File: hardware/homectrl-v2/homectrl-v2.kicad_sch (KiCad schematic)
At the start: 127 parts, among them J1 Barrel_Jack, J2 PUMP1_CONN, J3 PUMP2_CONN, J4 STEP_CONN, J5 USB_C_CONN, J6 SMS1_CONN, J7 ALS_CONN, J8 FSW1_CONN, Q1 AO3407A, Q2 2N7002, Q3 ZXMN3A01ZTA, Q4 ZXMN3A01ZTA, Q5 AO3400A, SW1 S3_RESET_SW, SW2 S3_BOOT_SW, U1 TPS5405DR, U2 MCP1826S, U3 DMP4065S-7, U4 ESP32-S3-WROOM-1, U5 TMC2209, U7 TPD4E001DRLR, U8 TPD2E001DRLR, U9 SI2347DS-T1-GE3

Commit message: misc work
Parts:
- removed R37: 13k, Resistor_SMD:R_0402_1005Metric, symbol Device:R
- removed R38: 20K, Resistor_SMD:R_0402_1005Metric, symbol Device:R
- Q3, Q4: footprint ZXMN3_DIO -> Package_TO_SOT_SMD:SOT-89-3
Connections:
- net MTR_DIR: now also U4.11 (IO18)
- net MTR_STEP: now also U4.10 (IO17)
- net S3_RXD: now also U4.12 (IO8)
- net S3_TXD: now also U4.15 (IO3)
- net SMS1_DATA: now also U4.6 (IO6), U4.7 (IO7); no longer U4.12 (IO8)
- net SMS2_DATA: no longer U4.17 (IO9)
- net STEP_DIAG: now also U4.17 (IO9)
- net STEP_ENN: now also U4.18 (IO10)
- net VCC_SENSE: no longer names the net of U4.4 (IO4)
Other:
- note added: "V = 12 ( 20 / 120 ) = 2 v V < 3V3"
- note removed: "V = 12 ( 20 / 120 ) = 2 v V = 3.3 ( 20 / 33 ) = 2 v V > 3V3"

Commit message: dasdf
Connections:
- net PUMP1_GATE is gone; now on net PUMP1_EN: R22.1
- net SMS1_DATA: now also U4.5 (IO5); no longer U4.6 (IO6), U4.7 (IO7)
- net SMS2_DATA: now also U4.6 (IO6)
- net VPLUG_SENSE: now also U4.4 (IO4); no longer U4.5 (IO5)
- net VPMP_EN: now also U4.9 (IO16)
- net PUMP1_EN: now reaches U4.8 (IO15)
- net PUMP2_GATE renamed PUMP2_EN
- net PUMP2_EN: now also U4.7 (IO7)
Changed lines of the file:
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@@
+		)
+	)
+	(global_label "VPMP_EN"
+		(shape input)
+		(at 259.08 236.22 180)
+		(fields_autoplaced yes)
+		(effects
+			(font
+				(size 1.27 1.27)
+			)
+			(justify right)
+		)
+		(property "Intersheetrefs" "${INTERSHEET_REFS}"
+			(at 247.5677 236.22 0)
+			(effects
+				(font
+					(size 1.27 1.27)
+				)
+				(justify right)
+				(hide yes)
+			)
 		)
 	)
@@
 		)
 	)
-	(global_label "VPLUG_SENSE"
-		(shape output)
-		(at 259.08 208.28 180)
-		(fields_autoplaced yes)
-		(effects
-			(font
-				(size 1.27 1.27)
-			)
-			(justify right)
-		)
-		(property "Intersheetrefs" "${INTERSHEET_REFS}"
-			(at 243.0925 208.28 0)
-			(effects
-				(font
-					(size 1.27 1.27)
-				)
-				(justify right)
-				(hide yes)
-			)
-		)
-	)
 	(global_label "MTR_STEP"
 		(shape input)
@@
 		)
 	)
+	(global_label "SMS2_DATA"
+		(shape input)
+		(at 259.08 210.82 180)
+		(fields_autoplaced yes)
+		(effects
+			(font
+				(size 1.27 1.27)
+			)
+			(justify right)
+		)
+		(property "Intersheetrefs" "${INTERSHEET_REFS}"
+			(at 245.6325 210.82 0)
+			(effects
+				(font
+					(size 1.27 1.27)
+				)
+				(justify right)
+				(hide yes)
+			)
+		)
+	)
 	(global_label "VPLUG"
 		(shape input)
@@
 				)
 				(justify left)
+				(hide yes)
+			)
+		)
+	)
+	(global_label "PUMP2_EN"
+		(shape input)
+		(at 259.08 213.36 180)
+		(fields_autoplaced yes)
+		(effects
+			(font
+				(size 1.27 1.27)
+			)
+			(justify right)
+		)
+		(property "Intersheetrefs" "${INTERSHEET_REFS}"
+			(at 246.1163 213.36 0)
+			(effects
+				(font
+					(size 1.27 1.27)
+				)
+				(justify right)
 				(hide yes)
 			)
@@
 		)
 	)
-	(global_label "PUMP2_GATE"
+	(global_label "PUMP2_EN"
 		(shape input)
 		(at 340.36 133.35 180)
@@
 		)
 		(property "Intersheetrefs" "${INTERSHEET_REFS}"
-			(at 325.4006 133.35 0)
+			(at 327.3963 133.35 0)
 			(effects
 				(font
@@
 		)
 	)
+	(global_label "SMS1_DATA"
+		(shape input)
+		(at 259.08 208.28 180)
+		(fields_autoplaced yes)
+		(effects
+			(font
+				(size 1.27 1.27)
+			)
+			(justify right)
+		)
+		(property "Intersheetrefs" "${INTERSHEET_REFS}"
+			(at 245.6325 208.28 0)
+			(effects
+				(font
+					(size 1.27 1.27)
+				)
+				(justify right)
+				(hide yes)
+			)
+		)
+	)
 	(global_label "I2C_DTA"
 		(shape input)
@@
 		)
 	)
+	(global_label "VPLUG_SENSE"
+		(shape output)
+		(at 259.08 205.74 180)
+		(fields_autoplaced yes)
+		(effects
+			(font
+				(size 1.27 1.27)
+			)
+			(justify right)
+		)
+		(property "Intersheetrefs" "${INTERSHEET_REFS}"
+			(at 243.0925 205.74 0)
+			(effects
+				(font
+					(size 1.27 1.27)
+				)
+				(justify right)
+				(hide yes)
+			)
+		)
+	)
 	(global_label "STEP_2A"
 		(shape input)
@@
 		)
 	)
+	(global_label "PUMP1_EN"
+		(shape input)
+		(at 259.08 233.68 180)
+		(fields_autoplaced yes)
+		(effects
+			(font
+				(size 1.27 1.27)
+			)
+			(justify right)
+		)
+		(property "Intersheetrefs" "${INTERSHEET_REFS}"
+			(at 246.1163 233.68 0)
+			(effects
+				(font
+					(size 1.27 1.27)
+				)
+				(justify right)
+				(hide yes)
+			)
+		)
+	)
 	(global_label "I2C_CLK"
 		(shape input)
@@
 		)
 	)
-	(global_label "SMS1_DATA"
-		(shape input)
-		(at 259.08 213.36 180)
-		(fields_autoplaced yes)
-		(effects
-			(font
-				(size 1.27 1.27)
-			)
-			(justify right)
-		)
-		(property "Intersheetrefs" "${INTERSHEET_REFS}"
-			(at 245.6325 213.36 0)
-			(effects
-				(font
-					(size 1.27 1.27)
-				)
-				(justify right)
-				(hide yes)
-			)
-		)
-	)
 	(global_label "VPMP"
 		(shape input)
@@
 		)
 	)
-	(global_label "PUMP1_GATE"
+	(global_label "PUMP1_EN"
 		(shape input)
 		(at 337.82 106.68 180)
@@
 		)
 		(property "Intersheetrefs" "${INTERSHEET_REFS}"
-			(at 322.8606 106.68 0)
+			(at 324.8563 106.68 0)
 			(effects
 				(font
@@
 			(effects
 				(font
-					(size 1.27 1.27)
-				)
-				(justify right)
-				(hide yes)
-			)
-		)
-	)
-	(global_label "SMS1_DATA"
-		(shape input)
-		(at 259.08 210.82 180)
-		(fields_autoplaced yes)
-		(effects
-			(font
-				(size 1.27 1.27)
-			)
-			(justify right)
-		)
-		(property "Intersheetrefs" "${INTERSHEET_REFS}"
-			(at 245.6325 210.82 0)
-			(effects
-				(font

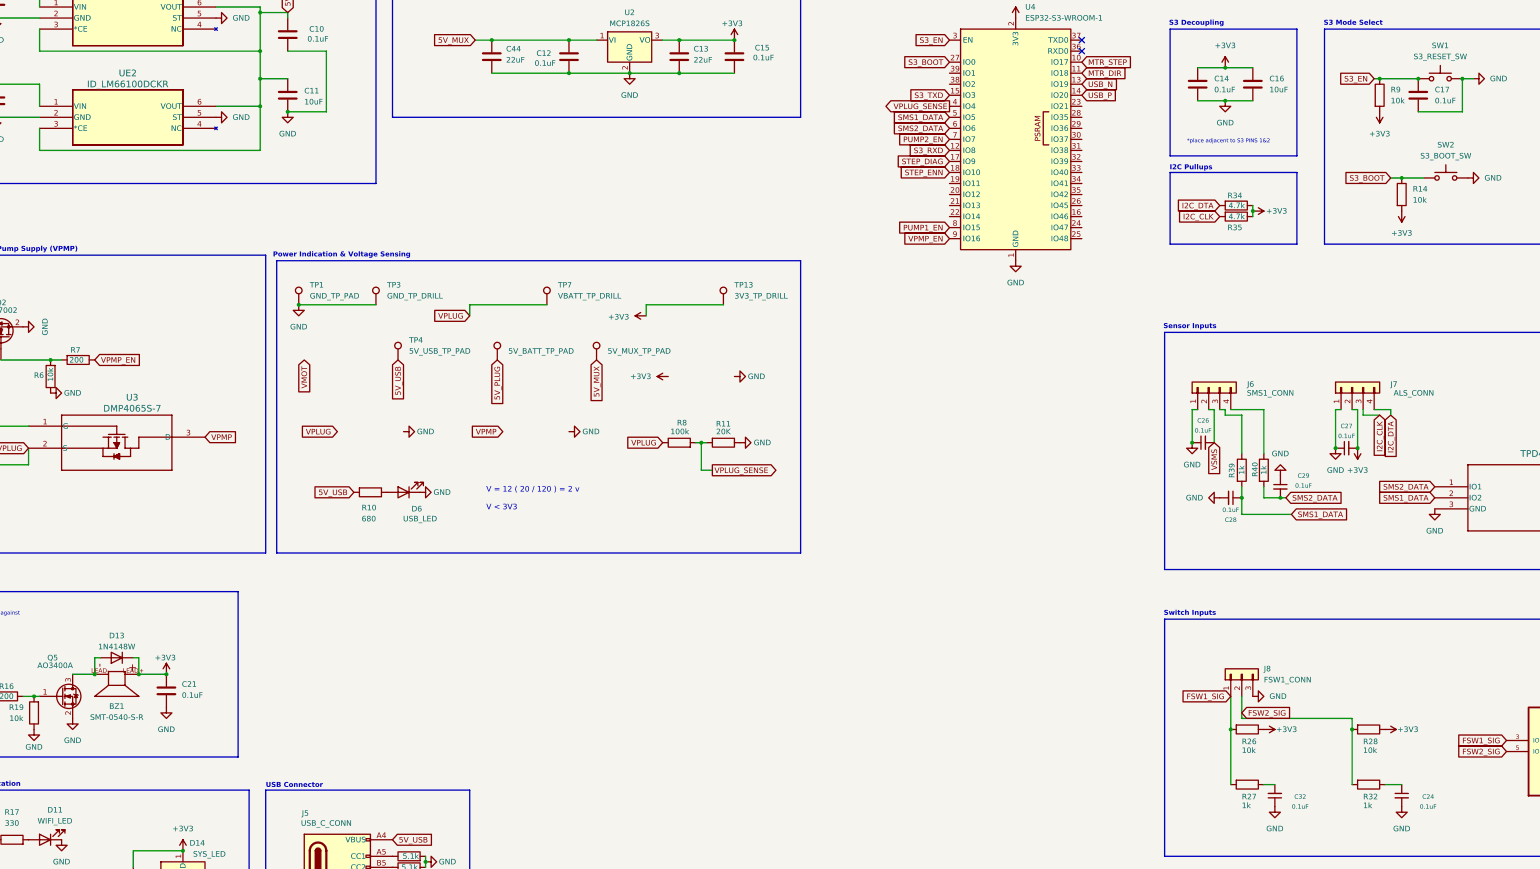
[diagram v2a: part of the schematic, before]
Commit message: more signal routing
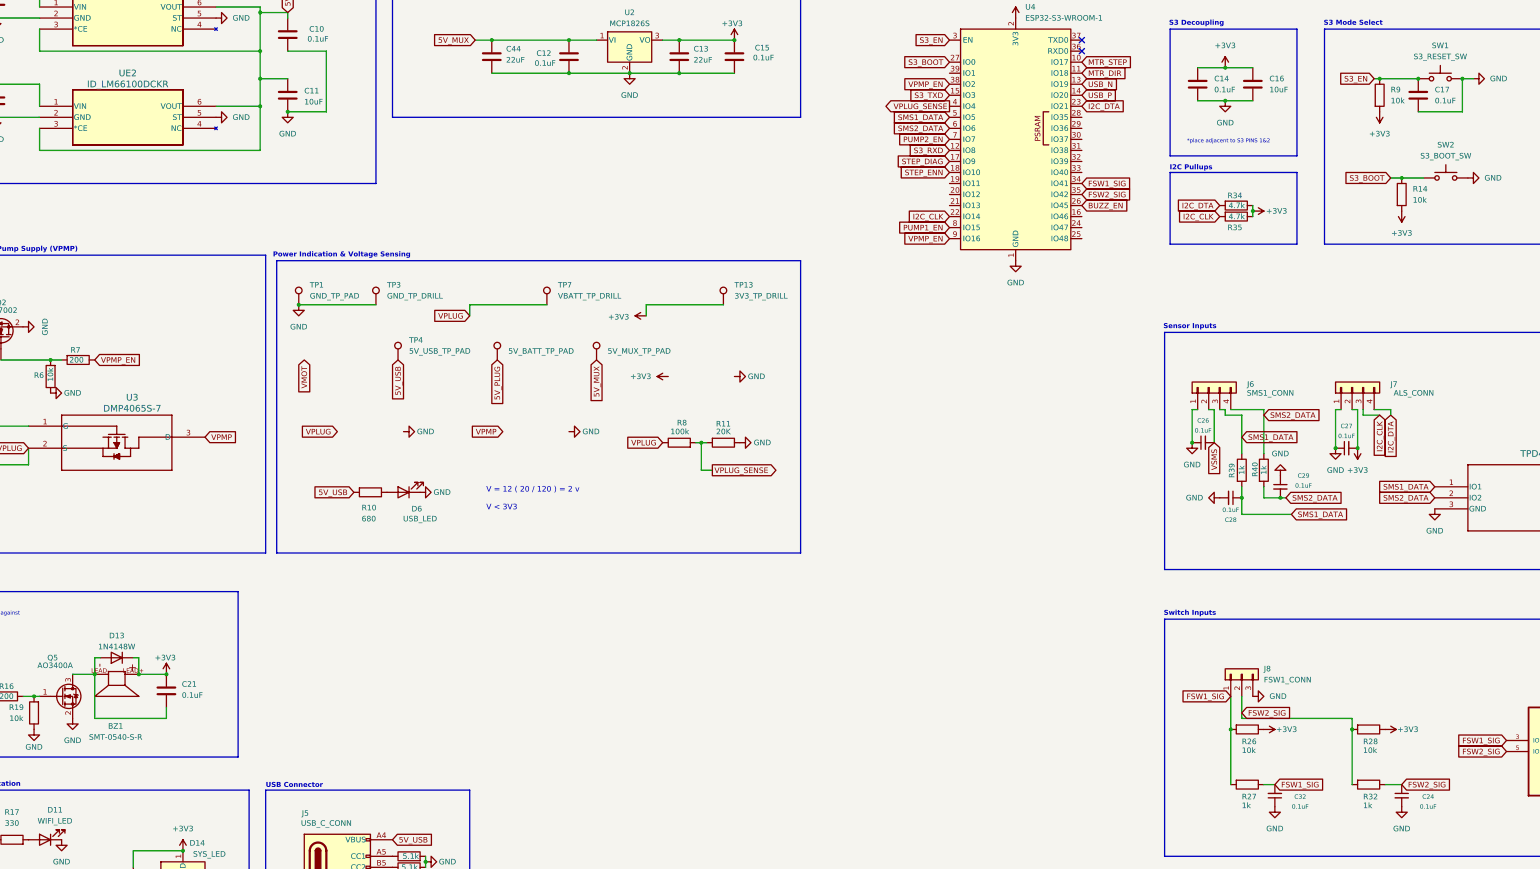
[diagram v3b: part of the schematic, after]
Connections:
- net BUZZ_EN: now also U4.26 (IO45)
- net FSW1_SIG: now also C32.2, R27.1, U4.34 (IO41)
- net FSW2_SIG: now also C24.1, R32.1, U4.35 (IO42)
- net GND: no longer C21.2
- net I2C_CLK: now also U4.22 (IO14)
- net I2C_DTA: now also U4.23 (IO21)
- net SMS1_DATA: now also J6.3 (Pin_3), R39.1, U7.1 (IO1); no longer U7.2 (IO2)
- net SMS2_DATA: now also J6.4 (Pin_4), R40.1, U7.2 (IO2); no longer U7.1 (IO1)
- net VPMP_EN: now also U4.38 (IO2)
- net at BZ1.LEAD-, D13.2 (A), Q5.3 (D): now also C21.2
